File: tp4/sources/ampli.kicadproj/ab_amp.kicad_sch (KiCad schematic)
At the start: 23 parts, among them Q201 BC337, Q202 BC337, Q203 BC327, Q204 BC327, Q205 BC337, Q206 TIP122, Q207 TIP127, U201 TL082

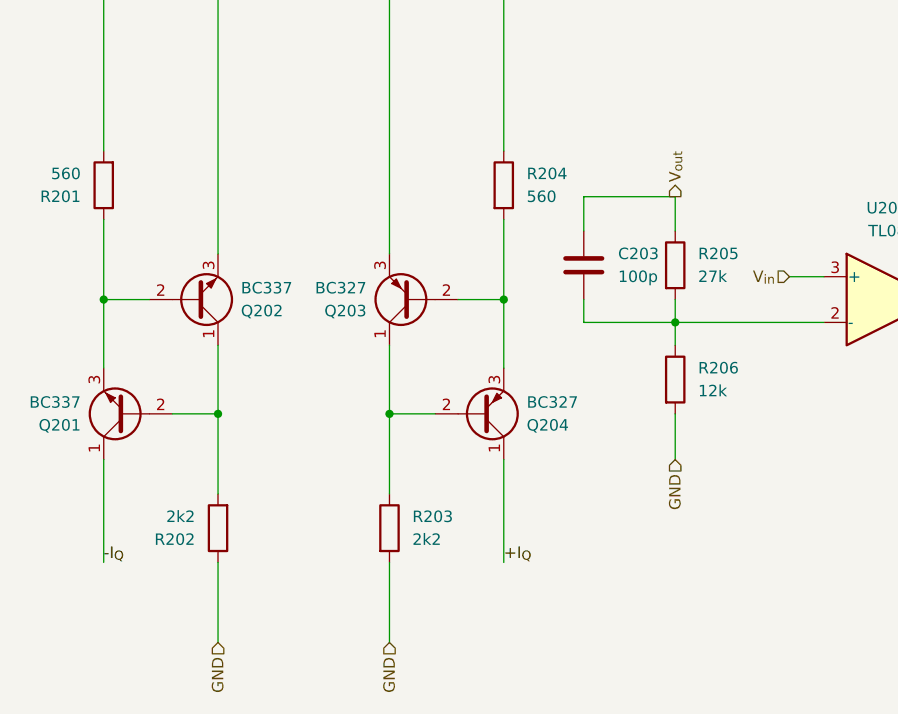
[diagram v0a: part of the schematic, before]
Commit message: tp4: Correcciones finales del esquematico para P=10W
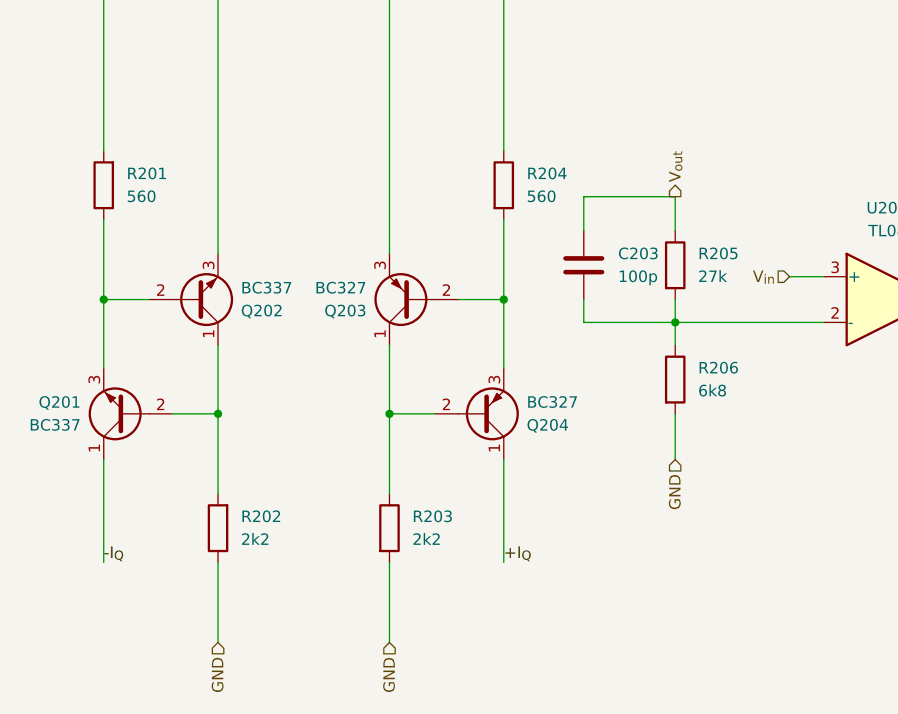
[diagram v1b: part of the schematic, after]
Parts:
- R206: value 12k -> 6k8
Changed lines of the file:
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@@
 		(fields_autoplaced yes)
 		(property "Reference" "R201"
-			(at 63.5 78.7401 0)
-			(show_name no)
-			(do_not_autoplace no)
-			(effects
-				(font
-					(size 1.27 1.27)
-				)
-				(justify left)
+			(at 68.58 76.1999 0)
+			(show_name no)
+			(do_not_autoplace no)
+			(effects
+				(font
+					(size 1.27 1.27)
+				)
+				(justify right)
 			)
 		)
 		(property "Value" "560"
-			(at 63.5 76.2001 0)
-			(show_name no)
-			(do_not_autoplace no)
-			(effects
-				(font
-					(size 1.27 1.27)
-				)
-				(justify left)
+			(at 68.58 78.7399 0)
+			(show_name no)
+			(do_not_autoplace no)
+			(effects
+				(font
+					(size 1.27 1.27)
+				)
+				(justify right)
 			)
 		)
@@
 					(reference "R201")
 					(unit 1)
+					(variant
+						(name "spk_10w")
+						(field
+							(name "Value")
+							(value "390")
+						)
+					)
 				)
 			)
@@
 		(fields_autoplaced yes)
 		(property "Reference" "R202"
-			(at 76.2 116.8401 0)
-			(show_name no)
-			(do_not_autoplace no)
-			(effects
-				(font
-					(size 1.27 1.27)
-				)
-				(justify left)
+			(at 81.28 114.2999 0)
+			(show_name no)
+			(do_not_autoplace no)
+			(effects
+				(font
+					(size 1.27 1.27)
+				)
+				(justify right)
 			)
 		)
 		(property "Value" "2k2"
-			(at 76.2 114.3001 0)
-			(show_name no)
-			(do_not_autoplace no)
-			(effects
-				(font
-					(size 1.27 1.27)
-				)
-				(justify left)
+			(at 81.28 116.8399 0)
+			(show_name no)
+			(do_not_autoplace no)
+			(effects
+				(font
+					(size 1.27 1.27)
+				)
+				(justify right)
 			)
 		)
@@
 		)
 		(property "Sim.Pins" "1=C 2=B 3=E"
+			(at 107.95 102.87 0)
+			(hide yes)
+			(show_name no)
+			(do_not_autoplace no)
+			(effects
+				(font
+					(size 1.27 1.27)
+				)
+			)
+		)
+		(property "Sim.Library" "/home/fpp/Documentos/UTN/ElectronicaAplicada2/tp4/sources/sim/bjt.lib"
+			(at 107.95 102.87 0)
+			(hide yes)
+			(show_name no)
+			(do_not_autoplace no)
+			(effects
+				(font
+					(size 1.27 1.27)
+				)
+			)
+		)
+		(property "Sim.Name" "BC327"
+			(at 107.95 102.87 0)
+			(hide yes)
+			(show_name no)
+			(do_not_autoplace no)
+			(effects
+				(font
+					(size 1.27 1.27)
+				)
+			)
+		)
+		(property "Sim.Type" "GUMMELPOON"
 			(at 107.95 102.87 0)
 			(hide yes)
@@
 					(reference "R205")
 					(unit 1)
+					(variant
+						(name "spk_10w")
+						(field
+							(name "Value")
+							(value "33k")
+						)
+					)
 				)
 			)
@@
 					(reference "R204")
 					(unit 1)
+					(variant
+						(name "spk_10w")
+						(field
+							(name "Value")
+							(value "390")
+						)
+					)
 				)
 			)
@@
 			)
 		)
-		(property "Value" "12k"
+		(property "Value" "6k8"
 			(at 132.08 100.3299 0)
 			(show_name no)
@@
 					(reference "R206")
 					(unit 1)
+					(variant
+						(name "spk_10w")
+						(field
+							(name "Value")
+							(value "3k9")
+						)
+					)
 				)
 			)
@@
 			)
 		)
+		(property "Sim.Library" "/home/fpp/Documentos/UTN/ElectronicaAplicada2/tp4/sources/sim/bjt.lib"
+			(at 76.2 90.17 0)
+			(hide yes)
+			(show_name no)
+			(do_not_autoplace no)
+			(effects
+				(font
+					(size 1.27 1.27)
+				)
+			)
+		)
+		(property "Sim.Name" "BC337"
+			(at 76.2 90.17 0)
+			(hide yes)
+			(show_name no)
+			(do_not_autoplace no)
+			(effects
+				(font
+					(size 1.27 1.27)
+				)
+			)
+		)
+		(property "Sim.Type" "GUMMELPOON"
+			(at 76.2 90.17 0)
+			(hide yes)
+			(show_name no)
+			(do_not_autoplace no)
+			(effects
+				(font
+					(size 1.27 1.27)
+				)
+			)
+		)
 		(pin "2"
 		)
@@
 		(fields_autoplaced yes)
 		(property "Reference" "Q201"
-			(at 63.5 104.1401 0)
+			(at 63.5 101.5999 0)
 			(show_name no)
 			(do_not_autoplace no)
@@
 		)
 		(property "Value" "BC337"
-			(at 63.5 101.6001 0)
+			(at 63.5 104.1399 0)
 			(show_name no)
 			(do_not_autoplace no)
@@
 		)
 		(property "Sim.Pins" "1=C 2=B 3=E"
+			(at 68.58 102.87 0)
+			(hide yes)
+			(show_name no)
+			(do_not_autoplace no)
+			(effects
+				(font
+					(size 1.27 1.27)
+				)
+			)
+		)
+		(property "Sim.Library" "/home/fpp/Documentos/UTN/ElectronicaAplicada2/tp4/sources/sim/bjt.lib"
+			(at 68.58 102.87 0)
+			(hide yes)
+			(show_name no)
+			(do_not_autoplace no)
+			(effects
+				(font
+					(size 1.27 1.27)
+				)
+			)
+		)
+		(property "Sim.Name" "BC337"
+			(at 68.58 102.87 0)
+			(hide yes)
+			(show_name no)
+			(do_not_autoplace no)
+			(effects
+				(font
+					(size 1.27 1.27)
+				)
+			)
+		)
+		(property "Sim.Type" "GUMMELPOON"
 			(at 68.58 102.87 0)
 			(hide yes)
@@
 			(at 182.88 90.17 0)
 			(hide yes)
+			(show_name no)
+			(do_not_autoplace no)
+			(effects
+				(font
+					(size 1.27 1.27)
+				)
+			)
+		)
+		(property "Sim.Library" "/home/fpp/Documentos/UTN/ElectronicaAplicada2/tp4/sources/sim/bjt.lib"
+			(at 182.88 90.17 0)
+			(hide yes)
+			(show_name no)
+			(do_not_autoplace no)
+			(effects
+				(font
+					(size 1.27 1.27)
+				)
+			)
+		)
+		(property "Sim.Name" "BC337"
+			(at 182.88 90.17 0)
+			(hide yes)
+			(show_name no)
+			(do_not_autoplace no)
+			(effects
+				(font
+					(size 1.27 1.27)
+				)
+			)
+		)
+		(property "Sim.Type" "GUMMELPOON"
+			(at 182.88 90.17 0)
+			(hide yes)
